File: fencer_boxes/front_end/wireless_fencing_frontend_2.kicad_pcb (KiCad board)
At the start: 2 copper layers, 16.8 x 22.8 mm, 18 parts, among them J1 Conn_01x03, J2 Conn_01x08, U2 AD8619

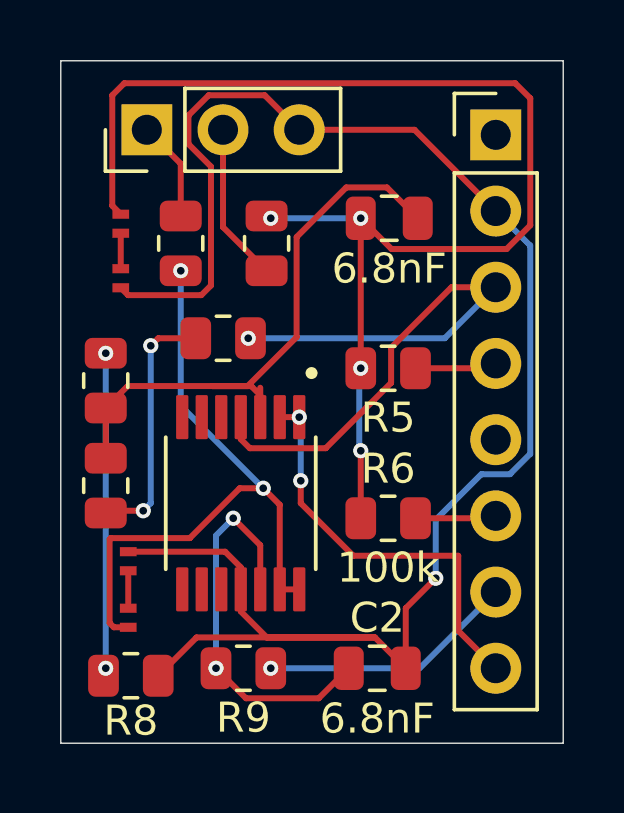
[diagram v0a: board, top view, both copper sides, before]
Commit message: fix lame drive component values
not sure these are final (higher f0 than i think is warranted),
but seem to work ok and what i had was bad (i.e. different than
intended and not working...)
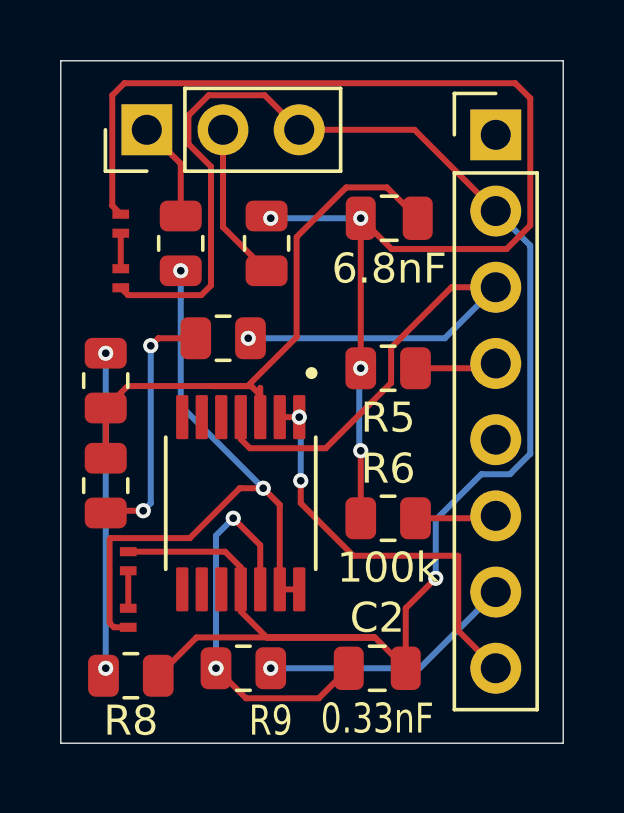
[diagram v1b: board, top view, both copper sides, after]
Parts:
- C2: value 6.8nF -> 0.33nF
- R9: value 20k -> 10k
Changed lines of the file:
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@@
 		(tags "resistor")
 		(property "Reference" "R9"
-			(at 0 -1.65 0)
-			(layer "F.SilkS")
-			(effects
-				(font
-					(size 1 1)
-					(thickness 0.15)
-				)
-			)
-		)
-		(property "Value" "20k"
-			(at 0 1.65 0)
-			(layer "F.Fab")
-			(hide yes)
-			(effects
-				(font
-					(size 1 1)
+			(at -0.9125 -1.75 0)
+			(layer "F.SilkS")
+			(effects
+				(font
+					(size 1 0.8)
+					(thickness 0.15)
+				)
+			)
+		)
+		(property "Value" "10k"
+			(at 1.0875 -1.75 0)
+			(layer "F.Fab")
+			(effects
+				(font
+					(size 1 0.8)
 					(thickness 0.15)
 				)
@@
 			)
 		)
-		(property "Value" "6.8nF"
+		(property "Value" "0.33nF"
 			(at 0 1.68 0)
 			(layer "F.SilkS")
 			(effects
 				(font
-					(size 1 1)
-					(thickness 0.15)
-				)
+					(size 1 0.8)
+					(thickness 0.15)
+				)
